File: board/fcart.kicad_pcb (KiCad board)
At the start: 2 copper layers, 100 x 62.7 mm, 99 parts, among them J1 USB_C_14P, J2 DM3D-SF, J3 JTAG, J4 SWD, J5 Famicom_cartridge, J6 MSD-4-A, J8 USB4085, SW1 PTS647SM70, U1 USBLC6-2SC6, U10 W9864G6KH-6, U2 TLV76133DCY, U3 TPS2116, U4 SN74ALVC164245DGG, U5 SN74ALVC164245DGG, U6 SN74ALVC164245DGG, U7 SN74ALVC164245DGG, U8 STM32F412RET6, U9 LCMXO2-4000HC-4TG144, Y1 ABS07-32.768KHZ-7, Y2 ABM8W-12.0000MHZ-8-B1U

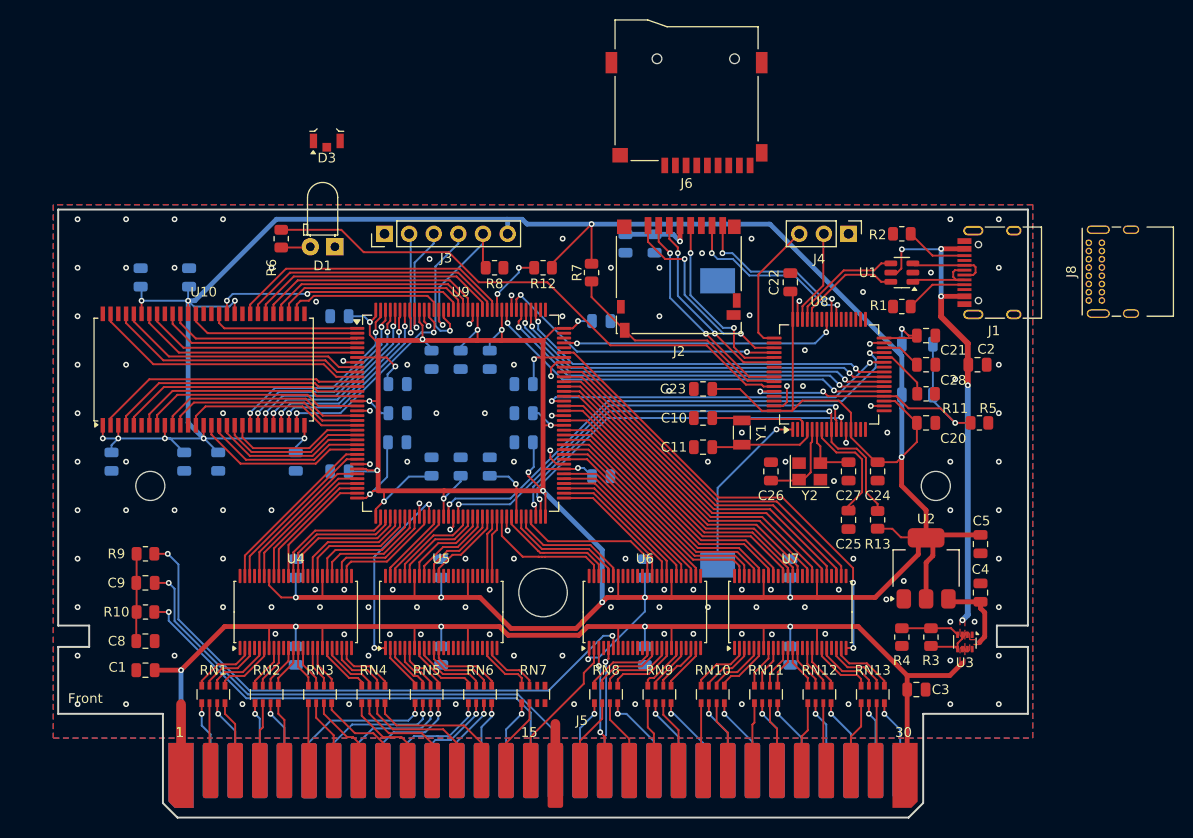
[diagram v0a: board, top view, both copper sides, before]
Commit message: Switch to fpga MAX10
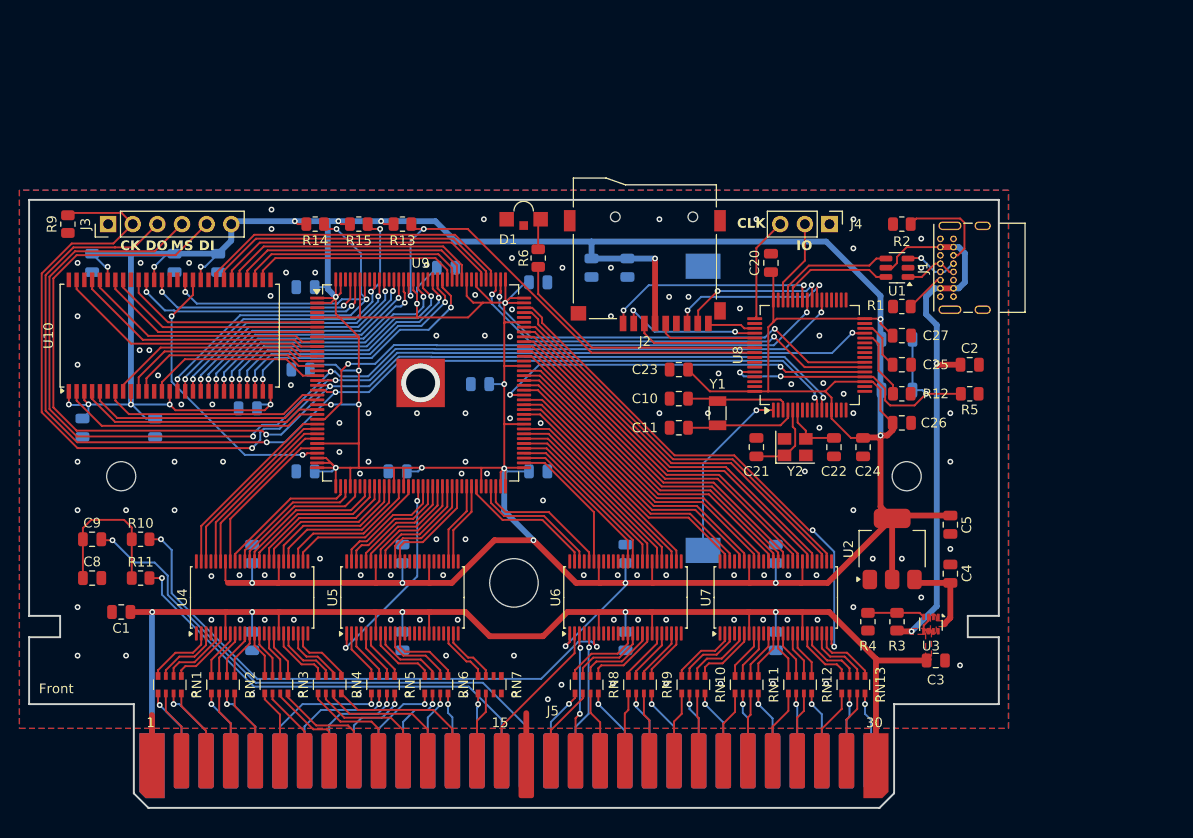
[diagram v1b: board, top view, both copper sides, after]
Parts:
- removed C42, C43, C44, C45, C46, C47, C48, C49, C50: 0.1u, Capacitor_SMD:C_0805_2012Metric
- removed D3: LTST-S326KGJRKT, LED_SMD:LED_LiteOn_LTST-S326
- removed J6: MSD-4-A, fcart:microSD_HC_Same_Sky_MSD-4-A
- removed J8: USB4085, Connector_USB:USB_C_Receptacle_GCT_USB4085
- removed R7: 10k, Resistor_SMD:R_0805_2012Metric
- removed R8: 5.1k, Resistor_SMD:R_0805_2012Metric
- added R14: 10k, Resistor_SMD:R_0805_2012Metric, F.Cu at (129.5, 70.5)
- added R15: 10k, Resistor_SMD:R_0805_2012Metric, F.Cu at (134.0, 70.5)
- C21, C22: value 0.1u -> 6.8p
- C25, C7: value 0.1u -> 4.7u
- C26, C27: value 6.8p -> 0.1u
- C28: value 4.7u -> 0.1u; moved to B.Cu
- C6: value 4.7u -> 0.1u
- D1: value LED 3mm -> LTST-S321KRKT; footprint LED_THT:LED_D3.0mm_Horizontal_O1.27mm_Z2.0mm -> fcart:LED_1208_Horizontal_3210Metric
- J1: value USB_C_14P -> USB4085; footprint Connector_USB:USB_C_Receptacle_HRO_TYPE-C-31-M-12 -> Connector_USB:USB_C_Receptacle_GCT_USB4085
- J2: value DM3D-SF -> MSD-4-A; footprint Connector_Card:microSD_HC_Hirose_DM3D-SF -> fcart:microSD_HC_Same_Sky_MSD-4-A
- R10: value 100 -> 1k
- R11: value 10k -> 100
- R9: value 1k -> 5.1k
- U9: value LCMXO2-4000HC-4TG144 -> 10M04SCE144C8G; footprint Package_QFP:TQFP-144_20x20mm_P0.5mm -> Package_QFP:EQFP-144-1EP_20x20mm_P0.5mm_EP5x5mm
- moved R11 83.2 mm to (111.5, 107.0)
- moved R13 57.7 mm to (138.5, 70.5), turned to 0 degrees
- moved C32 46.2 mm to (106.5, 74.5), turned to -90 degrees
- moved C28 40.9 mm to (152.5, 76.5)
- moved R12 39.2 mm to (190.0, 88.0), turned to 0 degrees
- moved C33 39.2 mm to (115.0, 74.5), turned to -90 degrees
- moved C34 36.5 mm to (119.5, 74.5), turned to -90 degrees
- moved C35 36.2 mm to (105.5, 91.5), turned to -90 degrees
- moved R9 34.9 mm to (104.0, 70.5), turned to 90 degrees
- moved C36 31.8 mm to (113.0, 91.5), turned to -90 degrees
- moved J3 28.5 mm to (108.2, 70.5)
- moved R6 26.6 mm to (152.5, 74.0), turned to -90 degrees
- moved C37 25.7 mm to (122.5, 89.5), turned to 180 degrees
- moved C20 23.0 mm to (176.5, 74.5), turned to 90 degrees
- moved C21 20.9 mm to (175.0, 93.5), turned to -90 degrees
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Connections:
- C21 pad 1: +3V3 -> GND
- C21 pad 2: GND -> Net-(U8-PH0)
- C22 pad 1: +3V3 -> GND
- C22 pad 2: GND -> Net-(U8-PH1)
- C25 pad 1: GND -> Net-(U8-VCAP_1)
- C25 pad 2: Net-(U8-NRST) -> GND
- C26 pad 1: GND -> +3V3
- C26 pad 2: Net-(U8-PH0) -> GND
- C27 pad 1: GND -> +3V3
- C27 pad 2: Net-(U8-PH1) -> GND
- C28 pad 1: Net-(U8-VCAP_1) -> +3V3
- J1 pad A8: (no net) -> unconnected-(J1-SBU1-PadA8)
- J1 pad B8: (no net) -> unconnected-(J1-SBU2-PadB8)
- J2 pad 10: SD_DET -> GND
- J2 pad 9: GND -> SD_DET
- J3 pad 2: TDO -> TCK
- J3 pad 3: TDI -> TDO
- J3 pad 5: TCK -> TDI
- R10 pad 2: SND_IN_5V -> SND_SYN_5V
- R11 pad 1: Net-(U8-PB2) -> Net-(C8-Pad1)
- R11 pad 2: GND -> SND_IN_5V
- R12 pad 1: +3V3 -> Net-(U8-PB2)
- R12 pad 2: Net-(U9A-PT23D/BANK0/C/PROGRAMN) -> GND
- R9 pad 1: Net-(C8-Pad1) -> GND
- R9 pad 2: SND_SYN_5V -> TCK
- U10 pad 15: SDRAM_LDQM -> SDRAM_DQM
- U10 pad 39: SDRAM_UDQM -> SDRAM_DQM
- U8 pad 10: SPI_MISO -> TDO
- U8 pad 11: SPI_MOSI -> TDI
- U8 pad 21: QSPI_IRQ -> SPI_SCK
- U8 pad 22: QSPI_IO0 -> SPI_MISO
- U8 pad 23: QSPI_IO1 -> SPI_MOSI
- U8 pad 24: QSPI_IO2 -> unconnected-(U8-PC4-Pad24)
- U8 pad 25: QSPI_IO3 -> unconnected-(U8-PC5-Pad25)
- U8 pad 27: QSPI_CLK -> unconnected-(U8-PB1-Pad27)
- U8 pad 29: SPI_CLK -> TCK
- U8 pad 38: unconnected-(U8-PC7-Pad38) -> TMS
- U8 pad 42: unconnected-(U8-PA9-Pad42) -> SD_DAT2
- U8 pad 51: SD_DAT2 -> SD_DET
- U8 pad 52: QSPI_CS -> SD_DAT3
- U8 pad 55: unconnected-(U8-PB3-Pad55) -> LED
- U8 pad 56: unconnected-(U8-PB4-Pad56) -> SPI_CS
- U8 pad 57: SD_DAT3 -> unconnected-(U8-PB5-Pad57)
- U8 pad 58: SD_DET -> unconnected-(U8-PB6-Pad58)
- U8 pad 59: LED -> unconnected-(U8-PB7-Pad59)
- U8 pad 7: Net-(U8-NRST) -> unconnected-(U8-NRST-Pad7)
- U8 pad 9: SPI_CS -> unconnected-(U8-PC1-Pad9)
- U9 pad 1: SDRAM_UDQM -> +3V3
- U9 pad 10: SDRAM_DQ14 -> SDRAM_DQ13
- U9 pad 100: PPU_D4 -> PPU_D2
- U9 pad 101: GND -> PPU_D5
- U9 pad 102: +3V3 -> PPU_D3
- U9 pad 103: PPU_DIR -> +3V3
- U9 pad 104: unconnected-(U9A-PR3B/BANK1/C/R_GPLLC_IN/DQ0-Pad104) -> GND
- U9 pad 105: FPGA_CLK -> PPU_D4
- U9 pad 106: unconnected-(U9A-PR2B/BANK1/C/R_GPLLC_FB/DQ0-Pad106) -> PPU_DIR
- U9 pad 107: unconnected-(U9A-PR2A/BANK1/T/R_GPLLT_FB/DQ0-Pad107) -> +3V3
- U9 pad 109: unconnected-(U9A-PT28D/BANK0/C/DONE-Pad109) -> +3V3
- U9 pad 11: SDRAM_DQ15 -> SDRAM_DQ14
- U9 pad 110: unconnected-(U9A-PT28C/BANK0/T/INITN-Pad110) -> SPI_MOSI
- U9 pad 111: QSPI_IO3 -> SPI_MISO
- U9 pad 112: QSPI_IO2 -> SDRAM_A11
- U9 pad 113: QSPI_IO1 -> SDRAM_A9
- U9 pad 114: QSPI_IO0 -> SDRAM_A8
- U9 pad 115: QSPI_CS -> +3V3
- U9 pad 117: QSPI_IRQ -> +3V3
- U9 pad 118: +3V3 -> SDRAM_A7
- U9 pad 119: Net-(U9A-PT23D/BANK0/C/PROGRAMN) -> SDRAM_A6
- U9 pad 12: SDRAM_DQ0 -> SDRAM_DQ15
- U9 pad 120: SDRAM_A11 -> SDRAM_A5
- U9 pad 121: SDRAM_A9 -> SDRAM_A4
- U9 pad 122: SDRAM_A8 -> SDRAM_A3
- U9 pad 123: +3V3 -> SDRAM_A2
- U9 pad 124: GND -> SDRAM_A1
- U9 pad 125: SDRAM_A7 -> GND
- U9 pad 126: SDRAM_A6 -> SDRAM_A0
- U9 pad 127: SDRAM_A5 -> SDRAM_A10
- U9 pad 128: SDRAM_CLK -> +3V3
- U9 pad 129: unconnected-(U9A-NC-Pad129) -> SPI_CS
- U9 pad 13: SDRAM_DQ1 -> SDRAM_DQ4
- U9 pad 130: TMS -> SDRAM_BA1
- U9 pad 131: TCK -> SDRAM_BA0
- U9 pad 132: SDRAM_A4 -> SDRAM_CS
- U9 pad 133: SDRAM_A3 -> GND
- U9 pad 134: GND -> SDRAM_RAS
- U9 pad 135: +3V3 -> SDRAM_CAS
- U9 pad 136: TDI -> SDRAM_WE
- U9 pad 137: TDO -> GND
- U9 pad 138: SDRAM_A2 -> SDRAM_DQM
- U9 pad 139: SDRAM_A1 -> +3V3
- U9 pad 14: SDRAM_DQ2 -> SDRAM_DQ5
- U9 pad 140: SDRAM_A0 -> SDRAM_DQ9
- U9 pad 141: SDRAM_A10 -> SDRAM_DQ8
- U9 pad 142: SDRAM_BA1 -> GND
- U9 pad 143: SDRAM_BA0 -> +3V3
- U9 pad 15: SDRAM_DQ3 -> SDRAM_DQ6
- U9 pad 16: +3V3 -> TMS
- U9 pad 17: SDRAM_DQ4 -> SDRAM_DQ7
- U9 pad 18: GND -> TCK
- U9 pad 19: SDRAM_DQ5 -> TDI
- U9 pad 2: SDRAM_DQ8 -> +3V3
- U9 pad 20: SDRAM_DQ6 -> TDO
- U9 pad 21: SDRAM_DQ7 -> SDRAM_DQ3
- U9 pad 22: SDRAM_CS -> SDRAM_DQ2
- U9 pad 23: SDRAM_RAS -> +3V3
- U9 pad 24: SDRAM_CAS -> SDRAM_DQ1
- U9 pad 25: SDRAM_WE -> SDRAM_DQ0
- U9 pad 26: SDRAM_LDQM -> FPGA_CLK
- U9 pad 29: GND -> CPU_A12
- U9 pad 3: SDRAM_DQ9 -> GND
- U9 pad 30: +3V3 -> CPU_A10
- U9 pad 31: CPU_A12 -> +3V3
- U9 pad 32: CPU_A10 -> CPU_A13
- U9 pad 33: CPU_A13 -> SDRAM_CLK
- U9 pad 34: CPU_A9 -> +3V3
- U9 pad 35: CPU_A14 -> +3V3
- U9 pad 38: CPU_A8 -> CPU_A9
- U9 pad 39: CPU_A7 -> CPU_A14
- U9 pad 4: SDRAM_DQ10 -> GND
- U9 pad 40: CPU_A6 -> +3V3
- U9 pad 41: CPU_A5 -> CPU_A8
- U9 pad 42: CPU_A4 -> GND
- U9 pad 43: CPU_A3 -> CPU_A7
- U9 pad 44: CPU_A2 -> CPU_A6
- U9 pad 45: CPU_A1 -> CPU_A5
- U9 pad 46: GND -> CPU_A4
- U9 pad 47: CPU_A0 -> CPU_A3
- U9 pad 48: CPU_DIR -> CPU_A2
- U9 pad 49: CPU_D7 -> +3V3
- U9 pad 5: SDRAM_DQ11 -> +3V3
- U9 pad 50: CPU_D6 -> CPU_A1
- U9 pad 52: SPI_CLK -> CPU_A0
- U9 pad 54: SPI_MISO -> CPU_DIR
- U9 pad 55: CPU_D5 -> CPU_D7
- U9 pad 56: CPU_D4 -> CPU_D6
- U9 pad 57: CPU_D3 -> CPU_D5
- U9 pad 58: CPU_D2 -> CPU_D4
- U9 pad 59: CPU_D1 -> CPU_D3
- U9 pad 6: SDRAM_DQ12 -> SDRAM_DQ10
- U9 pad 60: CPU_D0 -> CPU_D2
- U9 pad 61: ROMSEL -> CPU_D1
- U9 pad 62: CPU_RW -> CPU_D0
- U9 pad 63: IRQ -> GND
- U9 pad 64: GND -> ROMSEL
- U9 pad 65: CIRAM_A10 -> CPU_RW
- U9 pad 66: +3V3 -> IRQ
- U9 pad 67: CIRAM_CE -> +3V3
- U9 pad 68: SND_SYN -> GND
- U9 pad 69: PPU_WR -> CIRAM_A10
- U9 pad 7: +3V3 -> SDRAM_DQ11
- U9 pad 70: SPI_CS -> CIRAM_CE
- U9 pad 71: SPI_MOSI -> +3V3
- U9 pad 73: PPU_RD -> +3V3
- U9 pad 74: PPU_A6 -> SND_SYN
- U9 pad 75: PPU_A7 -> PPU_WR
- U9 pad 76: PPU_A5 -> PPU_RD
- U9 pad 77: PPU_A8 -> PPU_A6
- U9 pad 78: PPU_A4 -> PPU_A7
- U9 pad 79: +3V3 -> PPU_A5
- U9 pad 8: GND -> SDRAM_DQ12
- U9 pad 80: GND -> PPU_A8
- U9 pad 81: PPU_A9 -> PPU_A4
- U9 pad 82: PPU_A3 -> +3V3
- U9 pad 83: PPU_A10 -> GND
- U9 pad 84: PPU_A2 -> PPU_A9
- U9 pad 85: PPU_A11 -> PPU_A3
- U9 pad 86: PPU_A1 -> PPU_A10
- U9 pad 87: PPU_A12 -> PPU_A2
- U9 pad 88: +3V3 -> SPI_SCK
- U9 pad 89: PPU_A0 -> PPU_A11
- U9 pad 9: SDRAM_DQ13 -> +3V3
- U9 pad 90: GND -> PPU_A1
- U9 pad 91: PPU_A13 -> PPU_A12
- U9 pad 92: PPU_D0 -> PPU_A0
- U9 pad 93: QSPI_CLK -> PPU_A13
- U9 pad 94: PPU_D7 -> +3V3
- U9 pad 95: PPU_D1 -> GND
- U9 pad 96: PPU_D6 -> PPU_D0
- U9 pad 97: PPU_D2 -> PPU_D7
- U9 pad 98: PPU_D5 -> PPU_D1
- U9 pad 99: PPU_D3 -> PPU_D6
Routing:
- net TCK: track 16.8 -> 126.5 mm, vias 1 -> 3
- net TDI: track 12.5 -> 119.9 mm, vias 1 -> 3
- net TDO: track 12.7 -> 117.1 mm, vias 1 -> 3
- net TMS: track 14.6 -> 118.9 mm, vias 1 -> 3
- net SDRAM_DQM: track 0.00 -> 57.0 mm, vias 0 -> 4
- net SPI_CLK: track 54.3 -> 0.00 mm, vias 2 -> 0
- net QSPI_IRQ: track 43.2 -> 0.00 mm, vias 2 -> 0
- net QSPI_IO0: track 42.1 -> 0.00 mm, vias 2 -> 0
- net QSPI_IO1: track 41.2 -> 0.00 mm, vias 2 -> 0
- net QSPI_IO2: track 40.4 -> 0.00 mm, vias 2 -> 0
- net SPI_SCK: track 0.00 -> 39.8 mm, vias 0 -> 2
- net QSPI_IO3: track 39.6 -> 0.00 mm, vias 2 -> 0
- net QSPI_CLK: track 37.2 -> 0.00 mm, vias 2 -> 0
- net GND: track 42.6 -> 10.6 mm, vias 135 -> 128
- net QSPI_CS: track 30.3 -> 0.00 mm, vias 2 -> 0
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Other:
- board text added: "CK"
- board text added: "CLK"
- board text added: "DI"
- board text added: "DO"
- board text added: "IO"
- board text added: "MS"

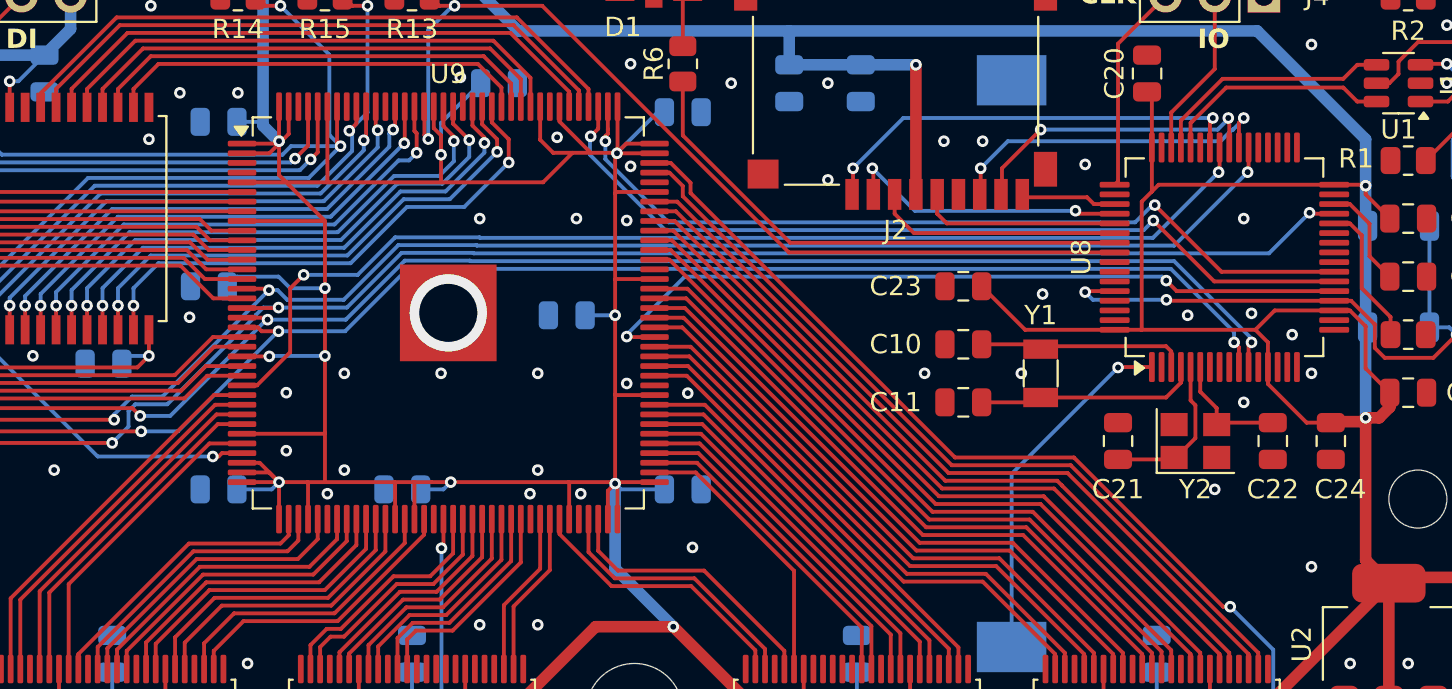
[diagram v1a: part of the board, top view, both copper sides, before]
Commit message: switch mcu to max 10 board
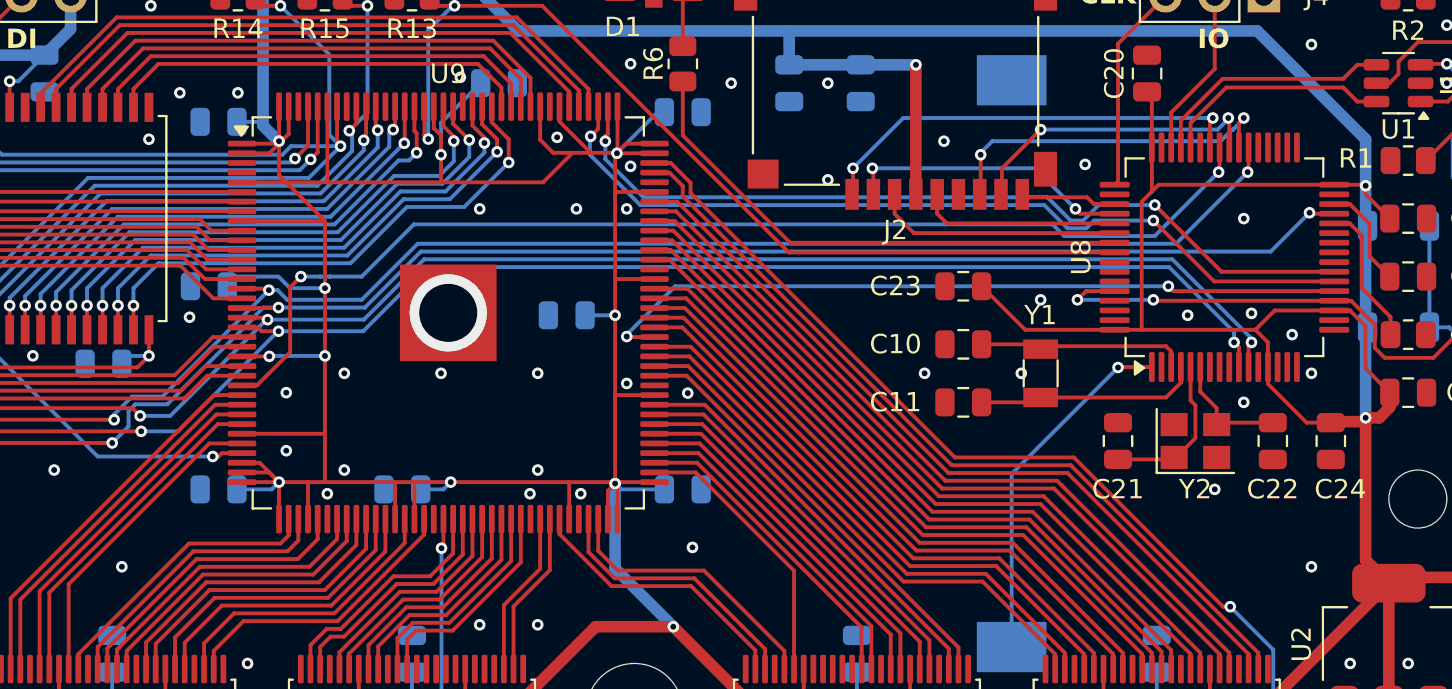
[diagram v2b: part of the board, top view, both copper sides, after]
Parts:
- R9: value 5.1k -> 1k
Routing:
- net BTN: track 33.8 -> 34.6 mm
- net FPGA_CLK: track 58.3 -> 58.8 mm

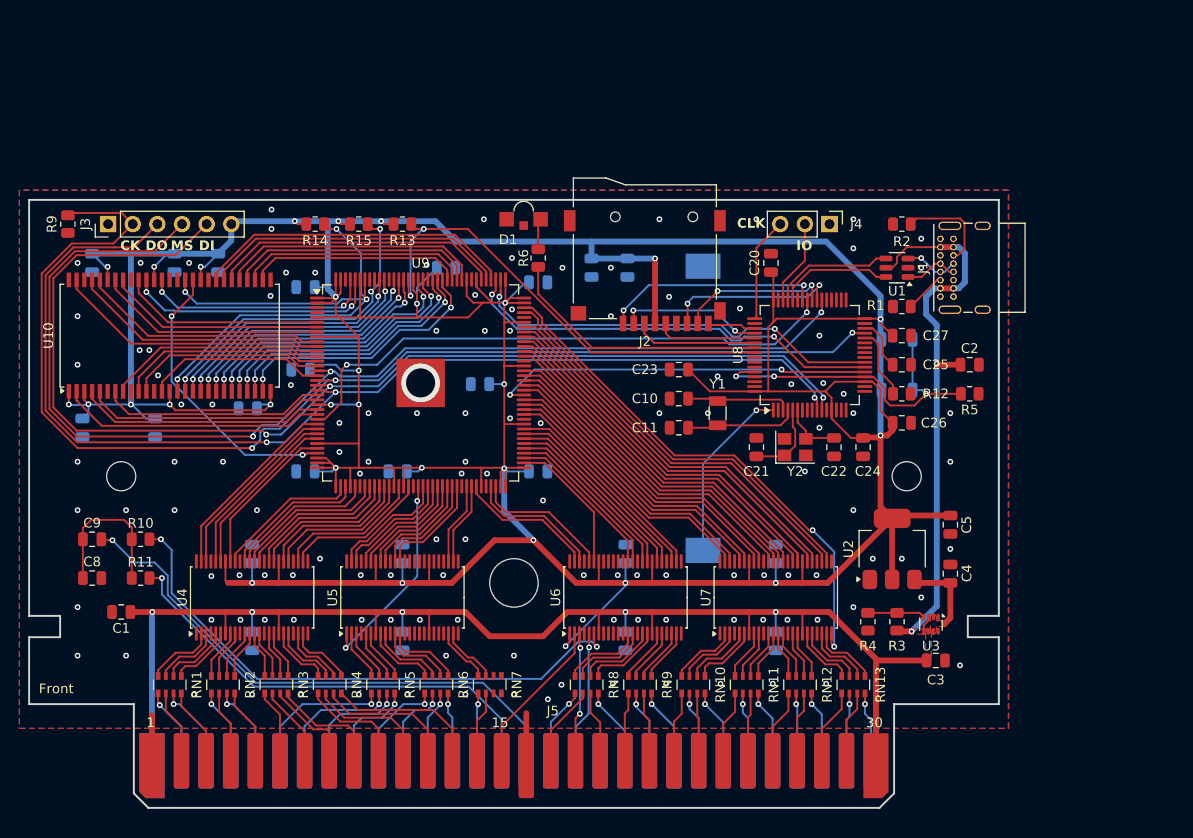
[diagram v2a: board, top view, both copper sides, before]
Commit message: New board design based on MachXO2
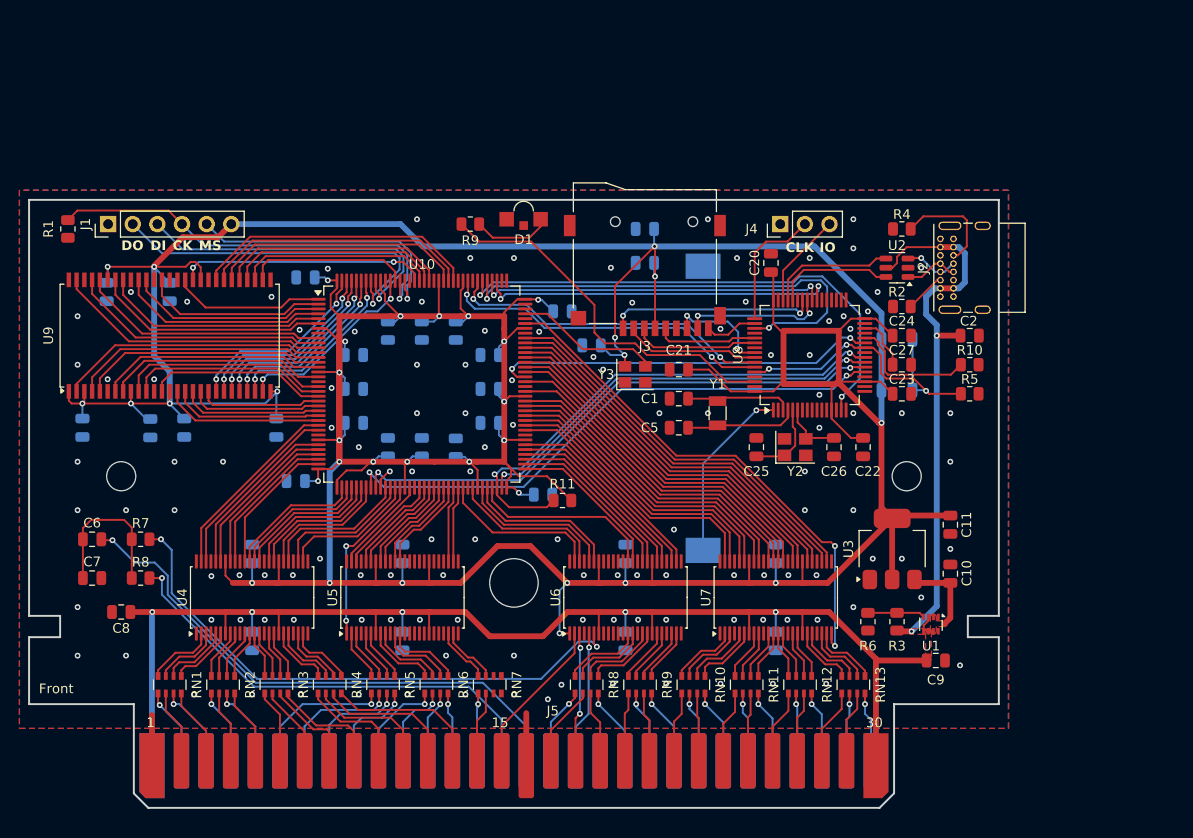
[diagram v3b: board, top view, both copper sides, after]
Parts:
- removed R14, R15: 10k, Resistor_SMD:R_0805_2012Metric
- removed the U9 at (140.4, 86.9)
- added C29: 0.1u, Capacitor_SMD:C_0805_2012Metric, B.Cu at (140.5, 81.5)
- added C32: 0.1u, Capacitor_SMD:C_0805_2012Metric, B.Cu at (133.5, 87.5)
- added C33: 0.1u, Capacitor_SMD:C_0805_2012Metric, B.Cu at (133.5, 91.0)
- added C34: 0.1u, Capacitor_SMD:C_0805_2012Metric, B.Cu at (137.0, 93.5)
- added C35: 0.1u, Capacitor_SMD:C_0805_2012Metric, B.Cu at (140.5, 93.5)
- added C36: 0.1u, Capacitor_SMD:C_0805_2012Metric, B.Cu at (144.0, 93.5)
- added C38: 0.1u, Capacitor_SMD:C_0805_2012Metric, B.Cu at (147.5, 87.5)
- added C39: 0.1u, Capacitor_SMD:C_0805_2012Metric, B.Cu at (147.5, 84.0)
- added C46: 0.1u, Capacitor_SMD:C_0805_2012Metric, B.Cu at (158.0, 83.0)
- added U10: LCMXO2-4000HC-4TG144C, Package_QFP:TQFP-144_20x20mm_P0.5mm, F.Cu at (140.5, 87.0)
- added Y3: ASE-50.000MHZ-LC, Oscillator:Oscillator_SMD_Abracon_ASE-4Pin_3.2x2.5mm, F.Cu at (162.5, 86.0)
- R1: renamed from R9; value 1k -> 5.1k
- moved R11 32.9 mm to (155.0, 99.0), turned to 180 degrees
- moved C50 28.1 mm to (153.0, 98.4), turned to 0 degrees
- moved C49 26.9 mm to (127.5, 97.0), turned to 180 degrees
- moved C47 23.7 mm to (155.0, 79.5), turned to 0 degrees
- moved C48 21.1 mm to (128.5, 76.0)
- moved C42 18.0 mm to (125.5, 91.5)
- moved C45 17.2 mm to (105.5, 91.5), turned to -90 degrees
- moved C30 16.8 mm to (137.0, 81.5), turned to -90 degrees
- moved C43 10.5 mm to (116.0, 91.5)
- moved C28 9.86 mm to (144.0, 81.5), turned to -90 degrees
- moved C31 8.60 mm to (133.5, 84.0), turned to 0 degrees
- moved C40 8.54 mm to (114.5, 77.5)
- moved R9 7.83 mm to (145.5, 70.5), turned to 180 degrees
- moved C41 7.62 mm to (108.0, 77.5)
- moved R10 7.62 mm to (197.0, 85.0)
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- renumbered C10 to C1, C4 to C10, C5 to C11, C23 to C21, C24 to C22, C26 to C23, C27 to C24, C21 to C25, C22 to C26, C25 to C27, C6 to C3, C29 to C37, C7 to C4, C32 to C40, C33 to C41, C34 to C42, C35 to C43, C36 to C44, C37 to C45, C38 to C47, C39 to C48, C40 to C49, C11 to C5, C41 to C50, C9 to C6, C8 to C7, C1 to C8, C3 to C9, J3 to J1, J1 to J2, J2 to J3, R12 to R10, R13 to R11, R1 to R2, R2 to R4, R4 to R6, R10 to R7, R11 to R8, R6 to R9, U3 to U1, U1 to U2, U2 to U3, U10 to U9
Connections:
- J1 pad 2: TCK -> TDO
- J1 pad 3: TDO -> TDI
- J1 pad 4: TMS -> TCK
- J1 pad 5: TDI -> TMS
- J4 pad 2: SWDIO -> SWCLK
- J4 pad 3: SWCLK -> SWDIO
- R1 pad 1: GND -> TCK
- R1 pad 2: TCK -> GND
- R11 pad 2: SPI_CS -> SPI_NCS
- U8 pad 10: TDO -> unconnected-(U8-PC2-Pad10)
- U8 pad 11: TDI -> unconnected-(U8-PC3-Pad11)
- U8 pad 15: unconnected-(U8-PA1-Pad15) -> QSPI_IO3
- U8 pad 20: BTN -> unconnected-(U8-PA4-Pad20)
- U8 pad 24: unconnected-(U8-PC4-Pad24) -> SPI_NCS
- U8 pad 26: unconnected-(U8-PB0-Pad26) -> BTN
- U8 pad 27: unconnected-(U8-PB1-Pad27) -> QSPI_CLK
- U8 pad 29: TCK -> unconnected-(U8-PB10-Pad29)
- U8 pad 38: TMS -> unconnected-(U8-PC7-Pad38)
- U8 pad 39: SD_DAT0 -> QSPI_IO2
- U8 pad 40: SD_DAT1 -> QSPI_IO0
- U8 pad 41: FPGA_CLK -> SD_DAT1
- U8 pad 50: unconnected-(U8-PA15-Pad50) -> SD_DET
- U8 pad 51: SD_DET -> QSPI_IO1
- U8 pad 52: SD_DAT3 -> unconnected-(U8-PC11-Pad52)
- U8 pad 55: LED -> unconnected-(U8-PB3-Pad55)
- U8 pad 56: SPI_CS -> SD_DAT0
- U8 pad 57: unconnected-(U8-PB5-Pad57) -> SD_DAT3
- U8 pad 58: unconnected-(U8-PB6-Pad58) -> QSPI_NCS
- U8 pad 59: unconnected-(U8-PB7-Pad59) -> FPGA_IRQ
- U8 pad 62: unconnected-(U8-PB9-Pad62) -> LED
- U9 pad 15: SDRAM_DQM -> SDRAM_LDQM
- U9 pad 39: SDRAM_DQM -> SDRAM_UDQM
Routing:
- net TMS: track 118.9 -> 29.2 mm, vias 3 -> 1
- net TDI: track 119.9 -> 34.2 mm, vias 3 -> 1
- net TCK: track 126.5 -> 44.1 mm, vias 3 -> 1
- net TDO: track 117.1 -> 37.3 mm, vias 3 -> 1
- net FPGA_CLK: track 58.8 -> 0.00 mm, vias 2 -> 0
- net SDRAM_DQM: track 57.0 -> 0.00 mm, vias 4 -> 0
- net QSPI_IO3: track 0.00 -> 53.9 mm, vias 0 -> 2
- net SPI_NCS: track 0.00 -> 52.5 mm, vias 0 -> 2
- net SPI_CS: track 50.2 -> 0.00 mm, vias 2 -> 0
- net QSPI_IO1: track 0.00 -> 49.2 mm, vias 0 -> 2
- net QSPI_CLK: track 0.00 -> 39.8 mm, vias 0 -> 2
- net QSPI_IO2: track 0.00 -> 37.1 mm, vias 0 -> 2
- net QSPI_IO0: track 0.00 -> 36.1 mm, vias 0 -> 2
- net FPGA_IRQ: track 0.00 -> 34.6 mm, vias 0 -> 2
- net QSPI_NCS: track 0.00 -> 33.8 mm, vias 0 -> 2
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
